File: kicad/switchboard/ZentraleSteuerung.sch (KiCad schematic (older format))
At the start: 2 parts

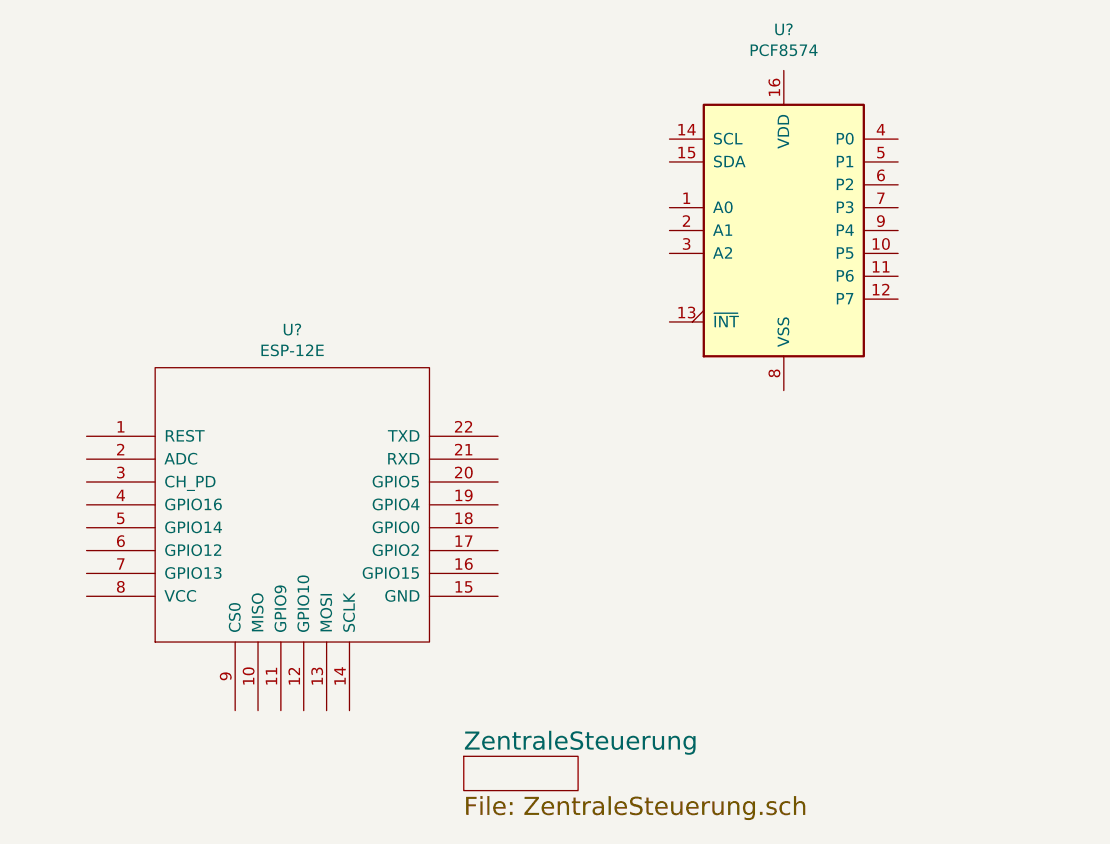
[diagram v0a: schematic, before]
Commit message: der switchboard schaltplan wurde angefangen
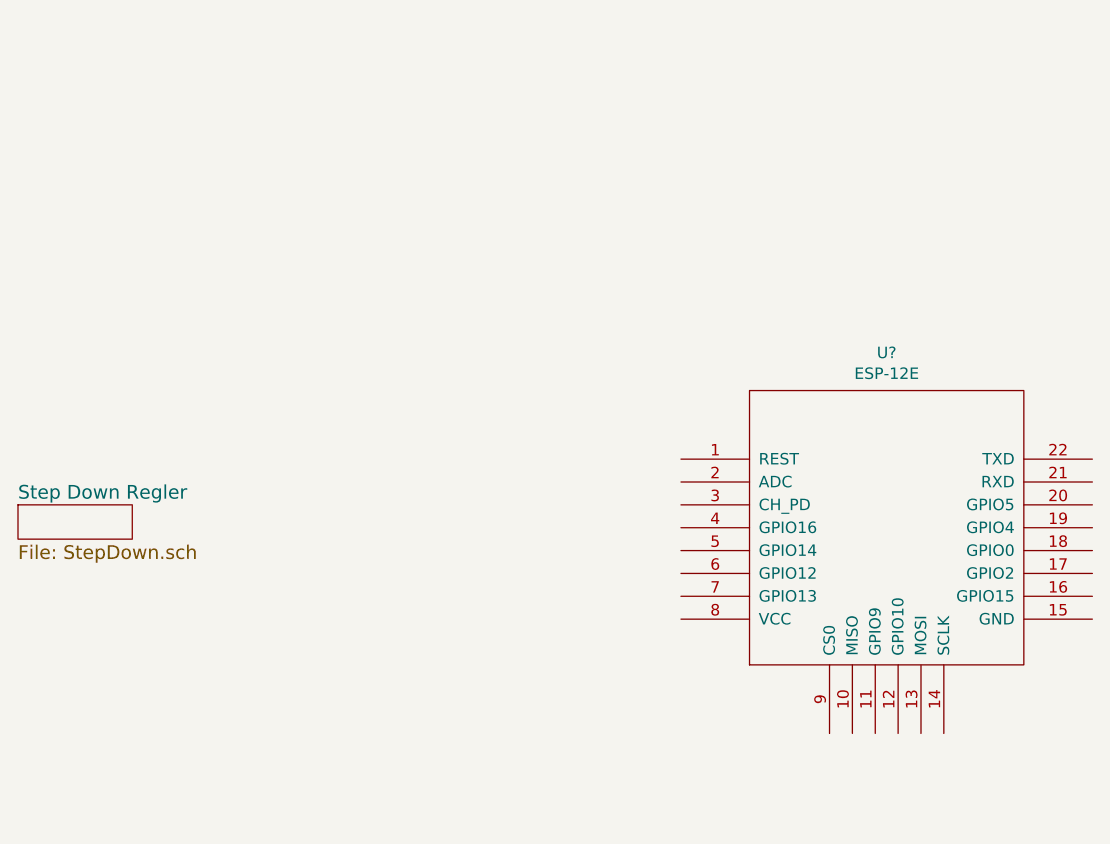
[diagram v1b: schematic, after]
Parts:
- removed U?: ESP-12E, symbol ESP-12E
- removed U?: PCF8574, symbol PCF8574
- added U?: ESP-12E, symbol ESP-12E
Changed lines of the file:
@@
 $Descr A4 11693 8268
 encoding utf-8
-Sheet 1 3
+Sheet 2 3
 Title ""
 Date ""
@@
 $Comp
 L ESP-12E U?
-U 1 1 581E4AF7
-P 4750 3250
-F 0 "U?" H 4750 4015 50  0000 C CNN
-F 1 "ESP-12E" H 4750 3924 50  0000 C CNN
-F 2 "" H 4750 3250 50  0001 C CNN
-F 3 "" H 4750 3250 50  0001 C CNN
-	1    4750 3250
-	1    0    0    -1
-$EndComp
-$Comp
-L PCF8574 U?
-U 1 1 581E4CAC
-P 6900 2050
-F 0 "U?" H 6900 2928 50  0000 C CNN
-F 1 "PCF8574" H 6900 2837 50  0000 C CNN
-F 2 "" H 6900 2050 50  0000 C CNN
-F 3 "" H 6900 2050 50  0000 C CNN
-	1    6900 2050
+U 1 1 581E5462
+P 7350 3350
+F 0 "U?" H 7350 4115 50  0000 C CNN
+F 1 "ESP-12E" H 7350 4024 50  0000 C CNN
+F 2 "" H 7350 3350 50  0001 C CNN
+F 3 "" H 7350 3350 50  0001 C CNN
+	1    7350 3350
 	1    0    0    -1
 $EndComp
 $Sheet
-S 5500 4350 500  150
-U 581E51AE
-F0 "ZentraleSteuerung" 79
-F1 "ZentraleSteuerung.sch" 79
+S 3550 3250 500  150
+U 581E5562
+F0 "Step Down Regler" 60
+F1 "StepDown.sch" 60
 $EndSheet
 $EndSCHEMATC
